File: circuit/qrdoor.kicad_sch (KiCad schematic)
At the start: 6 parts, among them J1 Screw_Terminal_01x02, J2 Screw_Terminal_01x02, J3 Screw_Terminal_01x08, J4 Screw_Terminal_01x02, J5 Conn_01x04, J6 Screw_Terminal_01x02

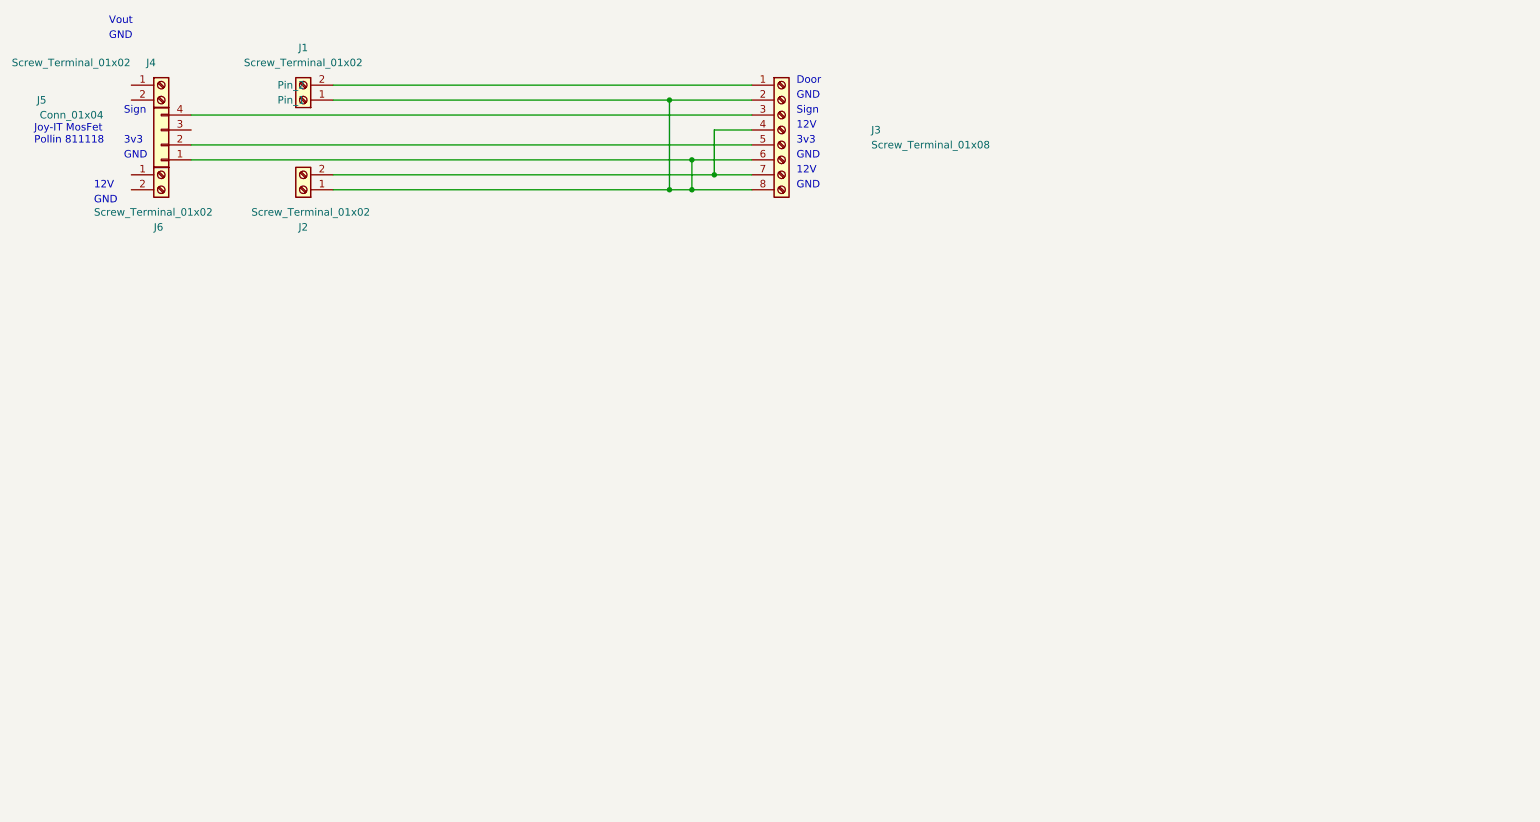
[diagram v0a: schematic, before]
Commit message: Kicad Schematic added, updated README
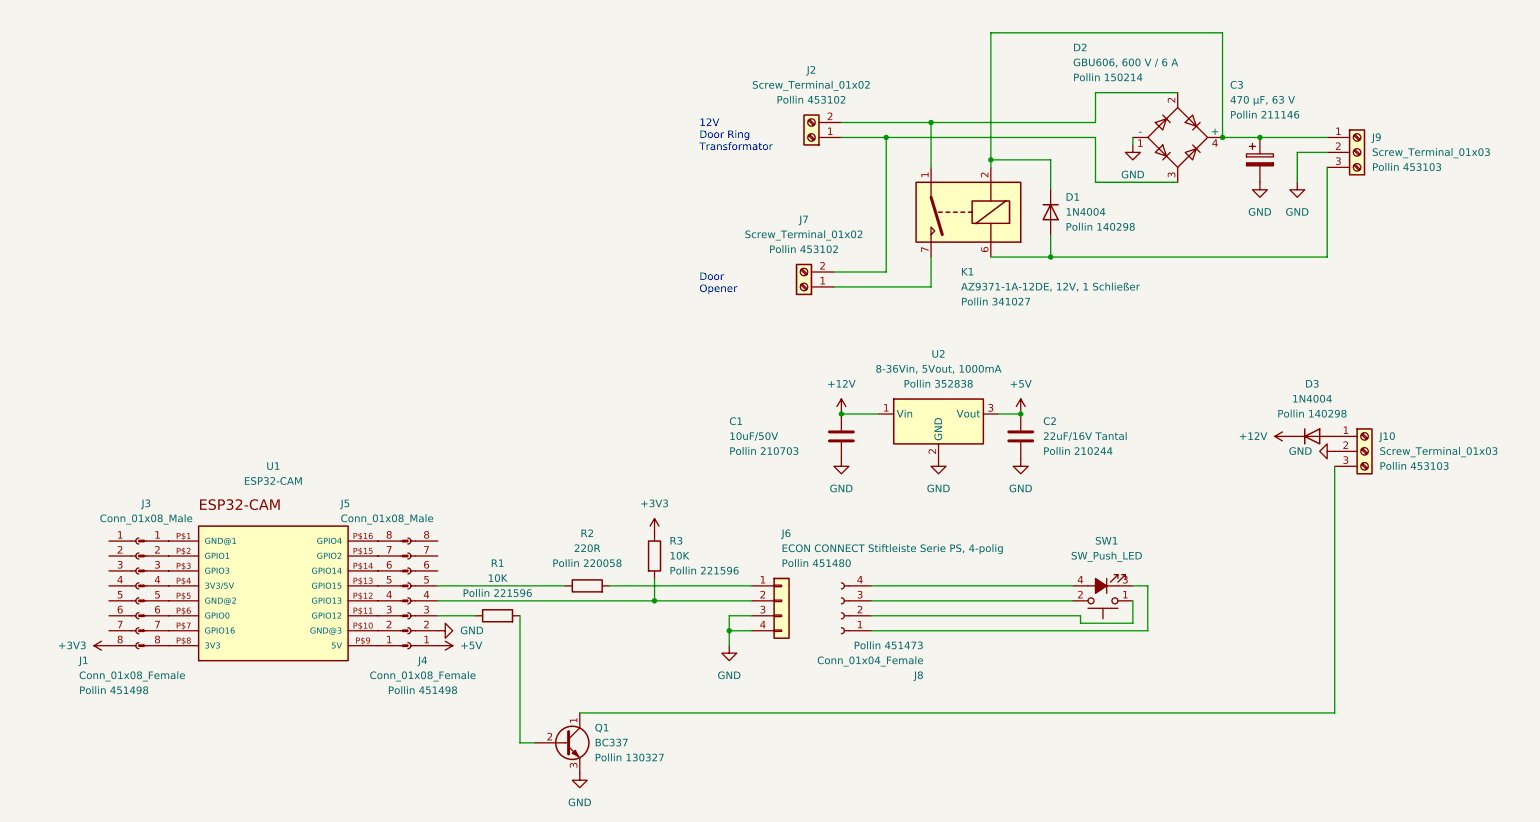
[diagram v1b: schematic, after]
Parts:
- removed J1, J4, J6: Screw_Terminal_01x02, symbol Connector:Screw_Terminal_01x02
- removed J3: Screw_Terminal_01x08, symbol Connector:Screw_Terminal_01x08
- removed J5: Conn_01x04, symbol Connector_Generic:Conn_01x04
- added C1: 10uF/50V, symbol Device:C
- added C2: 22uF/16V Tantal, symbol Device:C
- added C3: 470 µF, 63 V, symbol Device:C_Polarized
- added D1, D3: 1N4004, Diode_THT:D_DO-41_SOD81_P10.16mm_Horizontal, symbol Diode:1N4004
- added D2: GBU606, 600 V / 6 A, Diode_THT:Diode_Bridge_19.0x3.5x10.0mm_P5.0mm, symbol Diode_Bridge:B80C2300-1500A
- added J1, J4: Conn_01x08_Female, symbol Connector:Conn_01x08_Female
- added J10, J9: Screw_Terminal_01x03, symbol Connector:Screw_Terminal_01x03
- added J3, J5: Conn_01x08_Male, symbol Connector:Conn_01x08_Male
- added J6: ECON CONNECT Stiftleiste Serie PS, 4-polig, symbol Connector_Generic:Conn_01x04
- added J7: Screw_Terminal_01x02, symbol Connector:Screw_Terminal_01x02
- added J8: Conn_01x04_Female, symbol Connector:Conn_01x04_Female
- added K1: AZ9371-1A-12DE, 12V, 1 Schließer, Relay_THT:Relay_StandexMeder_DIP_LowProfile, symbol Relay:DIPxx-1Axx-11x
- added Q1: BC337, Package_TO_SOT_THT:TO-92_Inline, symbol Transistor_BJT:BC337
- added R1, R3: 10K, symbol Device:R
- added R2: 220R, symbol Device:R
- added SW1: SW_Push_LED, symbol Switch:SW_Push_LED
- added U1: ESP32-CAM, ESP32-CAM:ESP32-CAM, symbol ESP32-CAM:ESP32-CAM
- added U2: 8-36Vin, 5Vout, 1000mA, Converter_DCDC:Converter_DCDC_TRACO_TSR-1_THT, symbol Regulator_Switching:TSR_1-2450
- J2: Supplier (none) -> Pollin 453102
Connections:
- net at J2.1 (Pin_1): now also D2.3, J7.2 (Pin_2)
- net at J2.2 (Pin_2): now also D2.2, K1.1, K1.14
- new net: C3.1, D1.1 (K), D2.4 (+), J9.1 (Pin_1), K1.2
- new net: J4.3 (Pin_3), R1.1
- new net: J4.4 (Pin_4), J6.2 (Pin_2), R3.2
- new net: J4.5 (Pin_5), R2.1
- new net: D1.2 (A), J9.3 (Pin_3), K1.6
- new net: J7.1 (Pin_1), K1.7, K1.8
- new net: J3.1 (Pin_1), U1.P$1 (GND@1)
- new net: J5.2 (Pin_2), U1.P$10 (GND@3)
- new net: J5.3 (Pin_3), U1.P$11 (GPIO12)
- new net: J5.4 (Pin_4), U1.P$12 (GPIO13)
- new net: J5.5 (Pin_5), U1.P$13 (GPIO15)
- new net: J5.6 (Pin_6), U1.P$14 (GPIO14)
- new net: J5.7 (Pin_7), U1.P$15 (GPIO2)
- new net: J5.8 (Pin_8), U1.P$16 (GPIO4)
- new net: J3.2 (Pin_2), U1.P$2 (GPIO1)
- new net: J3.3 (Pin_3), U1.P$3 (GPIO3)
- new net: J3.4 (Pin_4), U1.P$4 (3V3/5V)
- new net: J3.5 (Pin_5), U1.P$5 (GND@2)
- new net: J3.6 (Pin_6), U1.P$6 (GPIO0)
- new net: J3.7 (Pin_7), U1.P$7 (GPIO16)
- new net: J3.8 (Pin_8), U1.P$8 (3V3)
- new net: J5.1 (Pin_1), U1.P$9 (5V)
- new net: J10.3 (Pin_3), Q1.1 (C)
- new net: Q1.2 (B), R1.2
- new net: J8.1 (Pin_1), SW1.3 (K)
- new net: J8.2 (Pin_2), SW1.1
- new net: J8.3 (Pin_3), SW1.2
- new net: J8.4 (Pin_4), SW1.4 (A)
- new net: D3.2 (A), J10.1 (Pin_1)
- new net: J6.1 (Pin_1), R2.2
- new net +12V: C1.1, D3.1 (K), U2.1 (Vin)
- new net +3V3: J1.8 (Pin_8), R3.1
- new net +5V: C2.1, J4.1 (Pin_1), U2.3 (Vout)
- new net GND: C1.2, C2.2, C3.2, D2.1 (-), J10.2 (Pin_2), J4.2 (Pin_2), J6.3 (Pin_3), J6.4 (Pin_4), J9.2 (Pin_2), Q1.3 (E), U2.2 (GND)
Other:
- note added: "12V Door Ring Transformator"
- note added: "Door Opener"
- note removed: "12V"
- note removed: "3v3"
- note removed: "Door"
- note removed: "GND"
- note removed: "Joy-IT MosFet Pollin 811118"
- note removed: "Sign"
- note removed: "Vout"
- moved on the sheet: J2
